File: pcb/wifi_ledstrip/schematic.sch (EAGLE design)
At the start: 44 parts, among them IC1 STM32F10XCXT6, Q1 8MHz

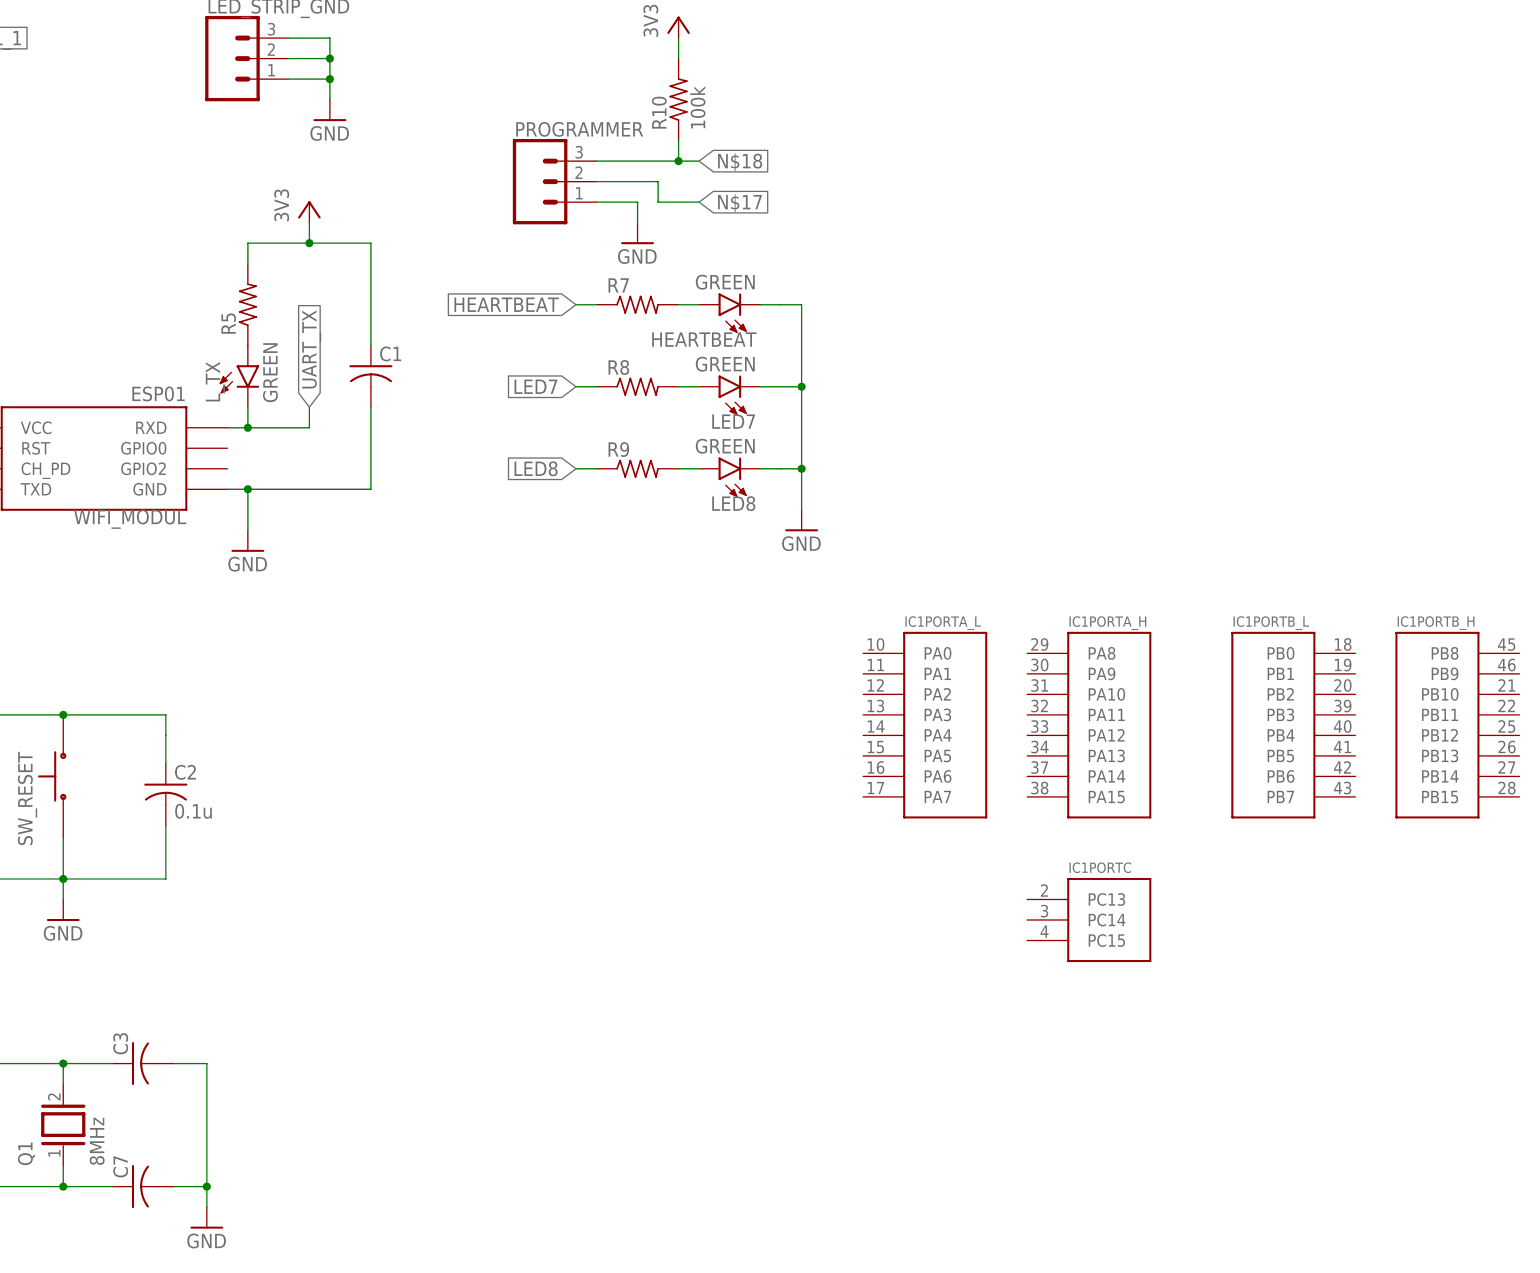
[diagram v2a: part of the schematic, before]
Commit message: xtal added and microcontroller pins connected - psu missing
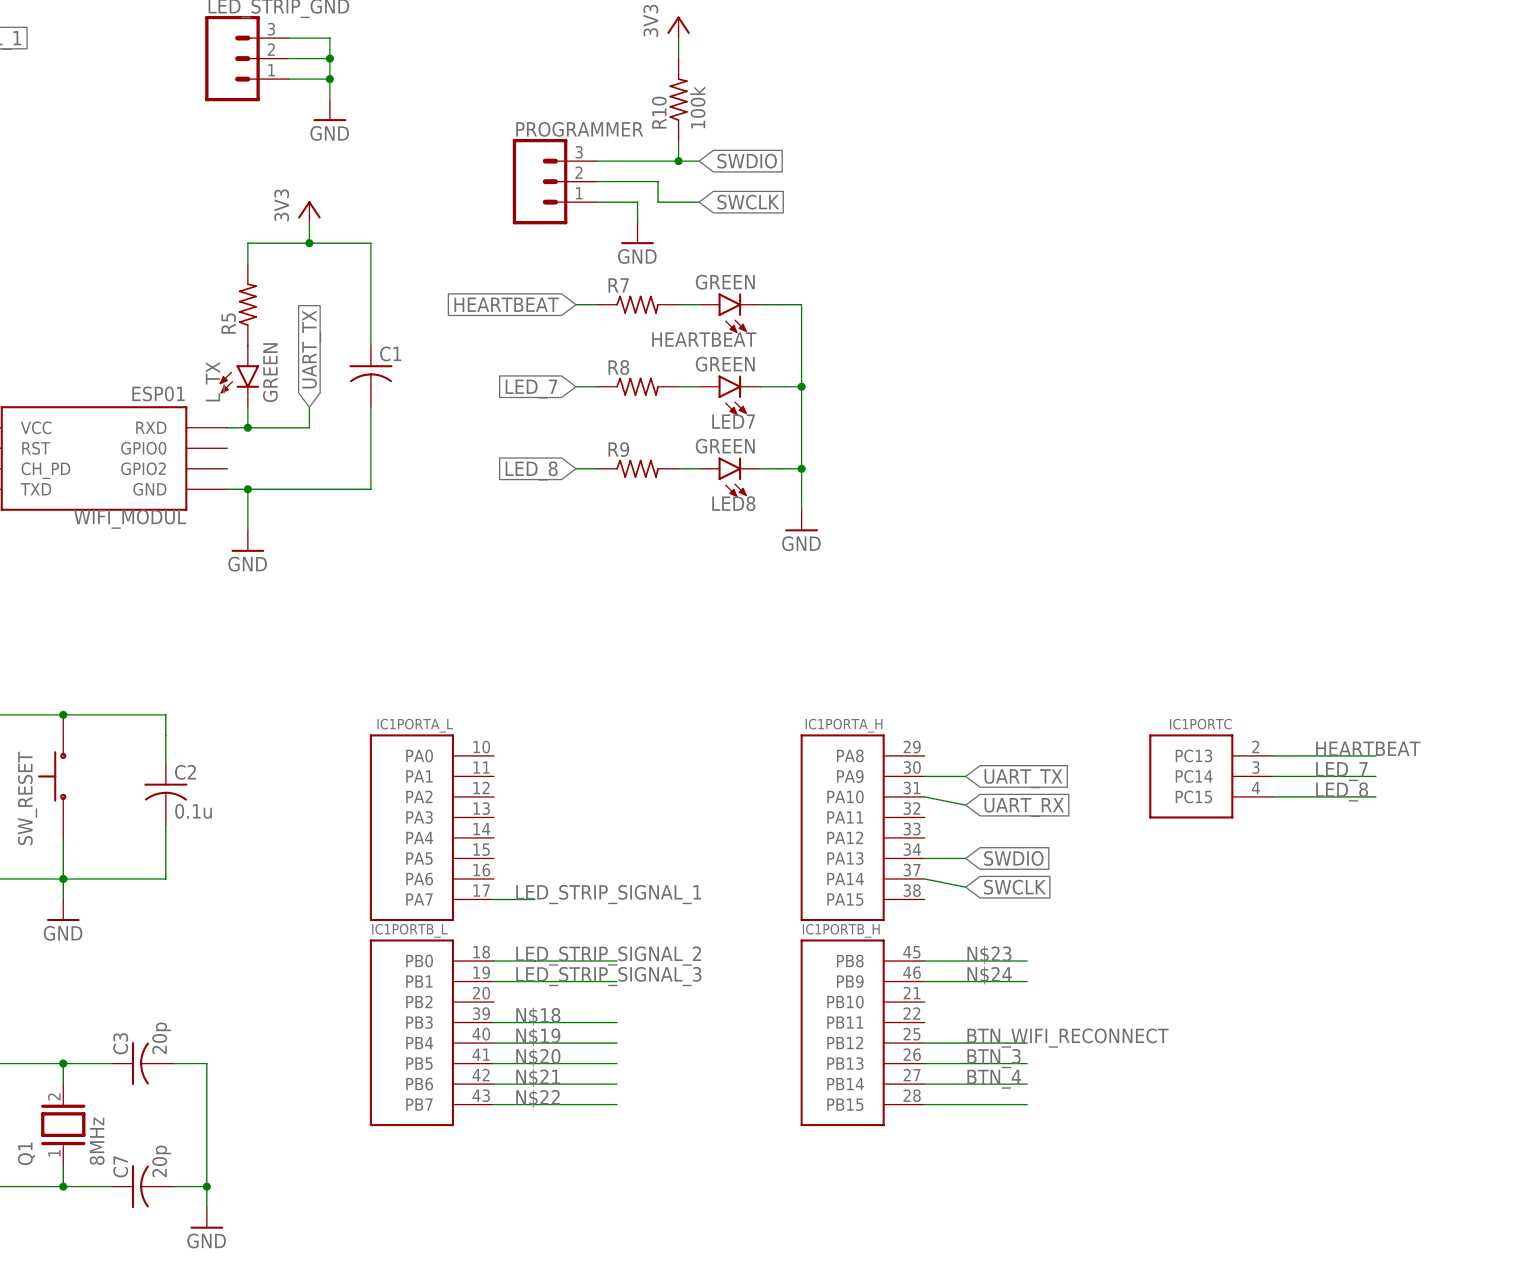
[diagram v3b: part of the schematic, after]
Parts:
- C3, C7: value (none) -> 20p
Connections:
- removed net LED7: R8.1
- removed net LED8: R9.1
- removed net N$17: PROGRAMMER.2
- new net LED_7: IC1PORTC.PC14, R8.1
- new net LED_8: IC1PORTC.PC15, R9.1
- new net N$19: IC1PORTB_L.PB4
- new net N$20: IC1PORTB_L.PB5
- new net N$21: IC1PORTB_L.PB6
- new net N$22: IC1PORTB_L.PB7
- new net N$23: IC1PORTB_H.PB8
- new net N$24: IC1PORTB_H.PB9
- new net N$27: IC1PORTB_H.PB15
- new net SWCLK: IC1PORTA_H.PA14, PROGRAMMER.2
- new net SWDIO: IC1PORTA_H.PA13, PROGRAMMER.3, R10.1
- net BTN_3: now also IC1PORTB_H.PB13
- net BTN_4: now also IC1PORTB_H.PB14
- net BTN_WIFI_RECONNECT: now also IC1PORTB_H.PB12
- net HEARTBEAT: now also IC1PORTC.PC13
- net LED_STRIP_SIGNAL_1: now also IC1PORTA_L.PA7
- net LED_STRIP_SIGNAL_2: now also IC1PORTB_L.PB0
- net LED_STRIP_SIGNAL_3: now also IC1PORTB_L.PB1
- net N$18: now also IC1PORTB_L.PB3; no longer PROGRAMMER.3, R10.1
- net UART_RX: now also IC1PORTA_H.PA10
- net UART_TX: now also IC1PORTA_H.PA9
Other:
- moved on the sheet: IC1PORTA_H, IC1PORTA_L, IC1PORTB_H, IC1PORTB_L, IC1PORTC
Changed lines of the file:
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@@
 <part name="P+13" library="supply1" library_urn="urn:adsk.eagle:library:371" deviceset="VCC" device="" value="3V3"/>
 <part name="Q1" library="special" library_urn="urn:adsk.eagle:library:367" deviceset="XTAL/S" device="" package3d_urn="urn:adsk.eagle:package:26647/2" value="8MHz"/>
-<part name="C3" library="rcl" library_urn="urn:adsk.eagle:library:334" deviceset="C-US" device="C1206" package3d_urn="urn:adsk.eagle:package:23618/2"/>
-<part name="C7" library="rcl" library_urn="urn:adsk.eagle:library:334" deviceset="C-US" device="C1206" package3d_urn="urn:adsk.eagle:package:23618/2"/>
+<part name="C3" library="rcl" library_urn="urn:adsk.eagle:library:334" deviceset="C-US" device="C1206" package3d_urn="urn:adsk.eagle:package:23618/2" value="20p"/>
+<part name="C7" library="rcl" library_urn="urn:adsk.eagle:library:334" deviceset="C-US" device="C1206" package3d_urn="urn:adsk.eagle:package:23618/2" value="20p"/>
 <part name="GND16" library="supply1" library_urn="urn:adsk.eagle:library:371" deviceset="GND" device=""/>
 <part name="R11" library="rcl" library_urn="urn:adsk.eagle:library:334" deviceset="R-US_" device="R1206" package3d_urn="urn:adsk.eagle:package:23540/2" value="10k"/>
@@
 </plain>
 <instances>
-<instance part="IC1" gate="PORTA_L" x="220.98" y="-30.48"/>
-<instance part="IC1" gate="PORTA_H" x="241.3" y="-33.02"/>
-<instance part="IC1" gate="PORTB_L" x="264.16" y="-33.02"/>
-<instance part="IC1" gate="PORTB_H" x="284.48" y="-30.48"/>
+<instance part="IC1" gate="PORTA_L" x="160.02" y="-43.18" rot="MR0"/>
+<instance part="IC1" gate="PORTA_H" x="213.36" y="-45.72" rot="MR0"/>
+<instance part="IC1" gate="PORTB_L" x="157.48" y="-71.12"/>
+<instance part="IC1" gate="PORTB_H" x="210.82" y="-68.58"/>
 <instance part="IC1" gate="POWER" x="66.04" y="-48.26"/>
-<instance part="IC1" gate="PORTC" x="241.3" y="-55.88"/>
+<instance part="IC1" gate="PORTC" x="256.54" y="-38.1" rot="MR0"/>
 <instance part="IC1" gate="PORTD/OSC" x="86.36" y="-81.28"/>
 <instance part="IC1" gate="AN_POWER" x="66.04" y="-86.36" rot="R180"/>
@@
 <label x="83.82" y="53.34" size="1.778" layer="95" xref="yes"/>
 </segment>
+<segment>
+<pinref part="IC1" gate="PORTA_L" pin="PA7"/>
+<wire x1="167.64" y1="-53.34" x2="170.18" y2="-53.34" width="0.1524" layer="91"/>
+<wire x1="170.18" y1="-53.34" x2="172.72" y2="-53.34" width="0.1524" layer="91"/>
+<label x="170.18" y="-53.34" size="1.778" layer="95"/>
+</segment>
 </net>
 <net name="LED_STRIP_SIGNAL_2" class="0">
@@
 <label x="83.82" y="68.58" size="1.778" layer="95" xref="yes"/>
 </segment>
+<segment>
+<pinref part="IC1" gate="PORTB_L" pin="PB0"/>
+<wire x1="167.64" y1="-60.96" x2="172.72" y2="-60.96" width="0.1524" layer="91"/>
+<label x="170.18" y="-60.96" size="1.778" layer="95"/>
+<wire x1="172.72" y1="-60.96" x2="182.88" y2="-60.96" width="0.1524" layer="91"/>
+</segment>
 </net>
 <net name="LED_STRIP_SIGNAL_3" class="0">
@@
 <wire x1="73.66" y1="83.82" x2="83.82" y2="83.82" width="0.1524" layer="91"/>
 <label x="83.82" y="83.82" size="1.778" layer="95" xref="yes"/>
+</segment>
+<segment>
+<pinref part="IC1" gate="PORTB_L" pin="PB1"/>
+<wire x1="167.64" y1="-63.5" x2="170.18" y2="-63.5" width="0.1524" layer="91"/>
+<wire x1="170.18" y1="-63.5" x2="172.72" y2="-63.5" width="0.1524" layer="91"/>
+<label x="170.18" y="-63.5" size="1.778" layer="95"/>
+<wire x1="172.72" y1="-63.5" x2="182.88" y2="-63.5" width="0.1524" layer="91"/>
 </segment>
 </net>
@@
 <label x="43.18" y="17.78" size="1.778" layer="95" xref="yes"/>
 </segment>
+<segment>
+<pinref part="IC1" gate="PORTB_H" pin="PB12"/>
+<wire x1="220.98" y1="-71.12" x2="233.68" y2="-71.12" width="0.1524" layer="91"/>
+<label x="226.06" y="-71.12" size="1.778" layer="95"/>
+</segment>
 </net>
 <net name="BTN_3" class="0">
@@
 <label x="43.18" y="10.16" size="1.778" layer="95" xref="yes"/>
 </segment>
+<segment>
+<pinref part="IC1" gate="PORTB_H" pin="PB13"/>
+<wire x1="220.98" y1="-73.66" x2="233.68" y2="-73.66" width="0.1524" layer="91"/>
+<label x="226.06" y="-73.66" size="1.778" layer="95"/>
+</segment>
 </net>
 <net name="BTN_4" class="0">
@@
 <wire x1="38.1" y1="2.54" x2="43.18" y2="2.54" width="0.1524" layer="91"/>
 <label x="43.18" y="2.54" size="1.778" layer="95" xref="yes"/>
+</segment>
+<segment>
+<pinref part="IC1" gate="PORTB_H" pin="PB14"/>
+<wire x1="220.98" y1="-76.2" x2="233.68" y2="-76.2" width="0.1524" layer="91"/>
+<label x="226.06" y="-76.2" size="1.778" layer="95"/>
 </segment>
 </net>
@@
 <junction x="88.9" y="-2.54"/>
 <label x="83.82" y="-2.54" size="1.778" layer="95" rot="R180" xref="yes"/>
+</segment>
+<segment>
+<pinref part="IC1" gate="PORTA_H" pin="PA10"/>
+<wire x1="220.98" y1="-40.64" x2="226.06" y2="-41.656" width="0.1524" layer="91"/>
+<label x="226.06" y="-41.656" size="1.778" layer="95" xref="yes"/>
 </segment>
 </net>
@@
 <wire x1="144.78" y1="5.08" x2="144.78" y2="7.62" width="0.1524" layer="91"/>
 </segment>
+<segment>
+<pinref part="IC1" gate="PORTA_H" pin="PA9"/>
+<wire x1="220.98" y1="-38.1" x2="226.06" y2="-38.1" width="0.1524" layer="91"/>
+<label x="226.06" y="-38.1" size="1.778" layer="95" xref="yes"/>
+</segment>
 </net>
 <net name="N$8" class="0">
@@
 </segment>
 </net>
-<net name="LED7" class="0">
+<net name="LED_7" class="0">
 <segment>
 <pinref part="R8" gate="G$1" pin="1"/>
@@
 <label x="177.8" y="10.16" size="1.778" layer="95" rot="R180" xref="yes"/>
 </segment>
+<segment>
+<pinref part="IC1" gate="PORTC" pin="PC14"/>
+<wire x1="264.16" y1="-38.1" x2="276.86" y2="-38.1" width="0.1524" layer="91"/>
+<label x="269.24" y="-38.1" size="1.778" layer="95"/>
+</segment>
 </net>
 <net name="HEARTBEAT" class="0">
@@
 <label x="177.8" y="20.32" size="1.778" layer="95" rot="R180" xref="yes"/>
 </segment>
-</net>
-<net name="LED8" class="0">
+<segment>
+<pinref part="IC1" gate="PORTC" pin="PC13"/>
+<wire x1="264.16" y1="-35.56" x2="276.86" y2="-35.56" width="0.1524" layer="91"/>
+<label x="269.24" y="-35.56" size="1.778" layer="95"/>
+</segment>
+</net>
+<net name="LED_8" class="0">
 <segment>
 <pinref part="R9" gate="G$1" pin="1"/>
 <wire x1="177.8" y1="0" x2="180.34" y2="0" width="0.1524" layer="91"/>
 <label x="177.8" y="0" size="1.778" layer="95" rot="R180" xref="yes"/>
+</segment>
+<segment>
+<pinref part="IC1" gate="PORTC" pin="PC15"/>
+<wire x1="264.16" y1="-40.64" x2="276.86" y2="-40.64" width="0.1524" layer="91"/>
+<label x="269.24" y="-40.64" size="1.778" layer="95"/>
 </segment>
 </net>
@@
 </segment>
 </net>
-<net name="N$17" class="0">
+<net name="SWCLK" class="0">
 <segment>
 <pinref part="PROGRAMMER" gate="J$1" pin="2"/>
@@
 <label x="193.04" y="33.02" size="1.778" layer="95" xref="yes"/>
 </segment>
-</net>
-<net name="N$18" class="0">
+<segment>
+<pinref part="IC1" gate="PORTA_H" pin="PA14"/>
+<wire x1="220.98" y1="-50.8" x2="226.06" y2="-51.816" width="0.1524" layer="91"/>
+<label x="226.06" y="-51.816" size="1.778" layer="95" xref="yes"/>
+</segment>
+</net>
+<net name="SWDIO" class="0">
 <segment>
 <pinref part="PROGRAMMER" gate="J$1" pin="3"/>
@@
 <pinref part="R10" gate="G$1" pin="1"/>
 </segment>
-</net>
+<segment>
+<pinref part="IC1" gate="PORTA_H" pin="PA13"/>
+<wire x1="220.98" y1="-48.26" x2="226.06" y2="-48.26" width="0.1524" layer="91"/>
+<label x="226.06" y="-48.26" size="1.778" layer="95" xref="yes"/>
+</segment>
+</net>
+<net name="N$18" class="0">
+<segment>
+<pinref part="IC1" gate="PORTB_L" pin="PB3"/>
+<wire x1="167.64" y1="-68.58" x2="182.88" y2="-68.58" width="0.1524" layer="91"/>
+<label x="170.18" y="-68.58" size="1.778" layer="95"/>
+</segment>
+</net>
+<net name="N$19" class="0">
+<segment>
+<pinref part="IC1" gate="PORTB_L" pin="PB4"/>
+<wire x1="167.64" y1="-71.12" x2="182.88" y2="-71.12" width="0.1524" layer="91"/>
+<label x="170.18" y="-71.12" size="1.778" layer="95"/>
+</segment>
+</net>
+<net name="N$20" class="0">
+<segment>
+<pinref part="IC1" gate="PORTB_L" pin="PB5"/>
+<wire x1="167.64" y1="-73.66" x2="182.88" y2="-73.66" width="0.1524" layer="91"/>
+<label x="170.18" y="-73.66" size="1.778" layer="95"/>
+</segment>
+</net>
+<net name="N$21" class="0">
+<segment>
+<pinref part="IC1" gate="PORTB_L" pin="PB6"/>
+<wire x1="167.64" y1="-76.2" x2="182.88" y2="-76.2" width="0.1524" layer="91"/>
+<label x="170.18" y="-76.2" size="1.778" layer="95"/>
+</segment>
+</net>
+<net name="N$22" class="0">
+<segment>
+<pinref part="IC1" gate="PORTB_L" pin="PB7"/>
+<wire x1="167.64" y1="-78.74" x2="182.88" y2="-78.74" width="0.1524" layer="91"/>
+<label x="170.18" y="-78.74" size="1.778" layer="95"/>
+</segment>
+</net>
+<net name="N$23" class="0">
+<segment>
+<pinref part="IC1" gate="PORTB_H" pin="PB8"/>
+<wire x1="220.98" y1="-60.96" x2="233.68" y2="-60.96" width="0.1524" layer="91"/>
+<label x="226.06" y="-60.96" size="1.778" layer="95"/>
+</segment>
+</net>
+<net name="N$24" class="0">
+<segment>
+<pinref part="IC1" gate="PORTB_H" pin="PB9"/>
+<wire x1="220.98" y1="-63.5" x2="233.68" y2="-63.5" width="0.1524" layer="91"/>
+<label x="226.06" y="-63.5" size="1.778" layer="95"/>
+</segment>
+</net>
+<net name="N$27" class="0">
+<segment>
+<pinref part="IC1" gate="PORTB_H" pin="PB15"/>
+<wire x1="220.98" y1="-78.74" x2="233.68" y2="-78.74" width="0.1524" layer="91"/>
+</segment>
+</net>
